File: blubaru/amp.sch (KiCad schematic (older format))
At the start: 20 parts, among them J1 TPA6112

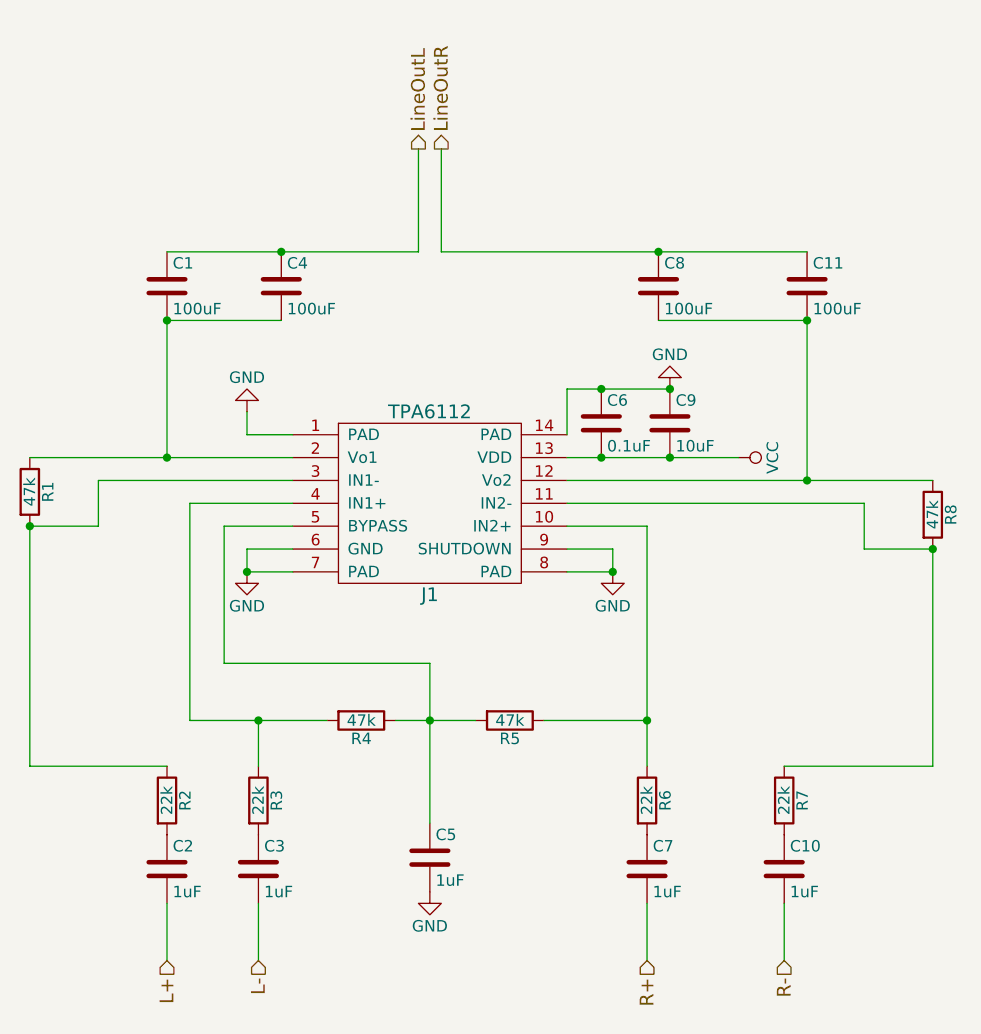
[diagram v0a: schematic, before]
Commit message: Put parts in the audio switch page.
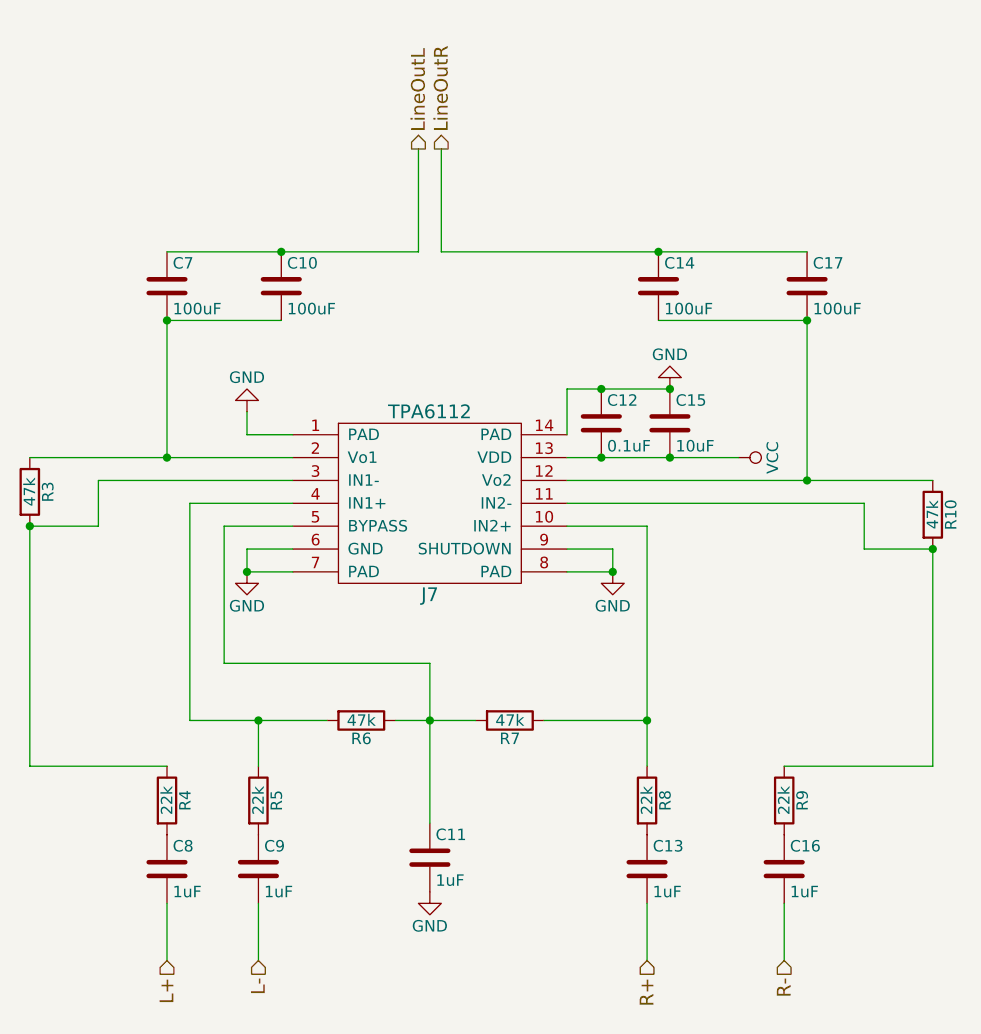
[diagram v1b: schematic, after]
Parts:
- renumbered C4 to C10, C5 to C11, C6 to C12, C7 to C13, C8 to C14, C9 to C15, C10 to C16, C11 to C17, C1 to C7, C2 to C8, C3 to C9, J1 to J7, R8 to R10, R1 to R3, R2 to R4, R3 to R5, R4 to R6, R5 to R7, R6 to R8, R7 to R9

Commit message: Create footprints for breakout boards
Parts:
- C10, C11, C12, C13, C14, C15, C16, C17, C7, C8, C9: footprint (none) -> Capacitors_THT:C_Disc_D5.0mm_W2.5mm_P2.50mm
- R10, R3, R4, R5, R6, R7, R8, R9: footprint (none) -> Resistors_THT:R_Axial_DIN0207_L6.3mm_D2.5mm_P7.62mm_Horizontal
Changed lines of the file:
@@
 encoding utf-8
 Sheet 8 8
-Title ""
-Date ""
+Title "Blubaru"
+Date "2017-02-28"
 Rev ""
 Comp ""
@@
 F 0 "C8" H 4175 5300 50  0000 L CNN
 F 1 "1uF" H 4175 5100 50  0000 L CNN
-F 2 "" H 4188 5050 50  0000 C CNN
+F 2 "Capacitors_THT:C_Disc_D5.0mm_W2.5mm_P2.50mm" H 4188 5050 50  0001 C CNN
 F 3 "" H 4150 5200 50  0000 C CNN
 	1    4150 5200
@@
 F 0 "C9" H 4575 5300 50  0000 L CNN
 F 1 "1uF" H 4575 5100 50  0000 L CNN
-F 2 "" H 4588 5050 50  0000 C CNN
+F 2 "Capacitors_THT:C_Disc_D5.0mm_W2.5mm_P2.50mm" H 4588 5050 50  0001 C CNN
 F 3 "" H 4550 5200 50  0000 C CNN
 	1    4550 5200
@@
 F 0 "C11" H 5325 5250 50  0000 L CNN
 F 1 "1uF" H 5325 5050 50  0000 L CNN
-F 2 "" H 5338 5000 50  0000 C CNN
+F 2 "Capacitors_THT:C_Disc_D5.0mm_W2.5mm_P2.50mm" H 5338 5000 50  0001 C CNN
 F 3 "" H 5300 5150 50  0000 C CNN
 	1    5300 5150
@@
 F 0 "C13" H 6275 5300 50  0000 L CNN
 F 1 "1uF" H 6275 5100 50  0000 L CNN
-F 2 "" H 6288 5050 50  0000 C CNN
+F 2 "Capacitors_THT:C_Disc_D5.0mm_W2.5mm_P2.50mm" H 6288 5050 50  0001 C CNN
 F 3 "" H 6250 5200 50  0000 C CNN
 	1    6250 5200
@@
 F 0 "C16" H 6875 5300 50  0000 L CNN
 F 1 "1uF" H 6875 5100 50  0000 L CNN
-F 2 "" H 6888 5050 50  0000 C CNN
+F 2 "Capacitors_THT:C_Disc_D5.0mm_W2.5mm_P2.50mm" H 6888 5050 50  0001 C CNN
 F 3 "" H 6850 5200 50  0000 C CNN
 	1    6850 5200
@@
 F 0 "C7" H 4175 2750 50  0000 L CNN
 F 1 "100uF" H 4175 2550 50  0000 L CNN
-F 2 "" H 4188 2500 50  0000 C CNN
+F 2 "Capacitors_THT:C_Disc_D5.0mm_W2.5mm_P2.50mm" H 4188 2500 50  0001 C CNN
 F 3 "" H 4150 2650 50  0000 C CNN
 	1    4150 2650
@@
 F 0 "C10" H 4675 2750 50  0000 L CNN
 F 1 "100uF" H 4675 2550 50  0000 L CNN
-F 2 "" H 4688 2500 50  0000 C CNN
+F 2 "Capacitors_THT:C_Disc_D5.0mm_W2.5mm_P2.50mm" H 4688 2500 50  0001 C CNN
 F 3 "" H 4650 2650 50  0000 C CNN
 	1    4650 2650
@@
 F 0 "C14" H 6325 2750 50  0000 L CNN
 F 1 "100uF" H 6325 2550 50  0000 L CNN
-F 2 "" H 6338 2500 50  0000 C CNN
+F 2 "Capacitors_THT:C_Disc_D5.0mm_W2.5mm_P2.50mm" H 6338 2500 50  0001 C CNN
 F 3 "" H 6300 2650 50  0000 C CNN
 	1    6300 2650
@@
 F 0 "C17" H 6975 2750 50  0000 L CNN
 F 1 "100uF" H 6975 2550 50  0000 L CNN
-F 2 "" H 6988 2500 50  0000 C CNN
+F 2 "Capacitors_THT:C_Disc_D5.0mm_W2.5mm_P2.50mm" H 6988 2500 50  0001 C CNN
 F 3 "" H 6950 2650 50  0000 C CNN
 	1    6950 2650
@@
 F 0 "C15" H 6375 3350 50  0000 L CNN
 F 1 "10uF" H 6375 3150 50  0000 L CNN
-F 2 "" H 6388 3100 50  0000 C CNN
+F 2 "Capacitors_THT:C_Disc_D5.0mm_W2.5mm_P2.50mm" H 6388 3100 50  0001 C CNN
 F 3 "" H 6350 3250 50  0000 C CNN
 	1    6350 3250
@@
 F 0 "C12" H 6075 3350 50  0000 L CNN
 F 1 "0.1uF" H 6075 3150 50  0000 L CNN
-F 2 "" H 6088 3100 50  0000 C CNN
+F 2 "Capacitors_THT:C_Disc_D5.0mm_W2.5mm_P2.50mm" H 6088 3100 50  0001 C CNN
 F 3 "" H 6050 3250 50  0000 C CNN
 	1    6050 3250
@@
 F 0 "R4" V 4230 4900 50  0000 C CNN
 F 1 "22k" V 4150 4900 50  0000 C CNN
-F 2 "" V 4080 4900 50  0000 C CNN
+F 2 "Resistors_THT:R_Axial_DIN0207_L6.3mm_D2.5mm_P7.62mm_Horizontal" V 4080 4900 50  0001 C CNN
 F 3 "" H 4150 4900 50  0000 C CNN
 	1    4150 4900
@@
 F 0 "R5" V 4630 4900 50  0000 C CNN
 F 1 "22k" V 4550 4900 50  0000 C CNN
-F 2 "" V 4480 4900 50  0000 C CNN
+F 2 "Resistors_THT:R_Axial_DIN0207_L6.3mm_D2.5mm_P7.62mm_Horizontal" V 4480 4900 50  0001 C CNN
 F 3 "" H 4550 4900 50  0000 C CNN
 	1    4550 4900
@@
 F 0 "R6" V 5080 4550 50  0000 C CNN
 F 1 "47k" V 5000 4550 50  0000 C CNN
-F 2 "" V 4930 4550 50  0000 C CNN
+F 2 "Resistors_THT:R_Axial_DIN0207_L6.3mm_D2.5mm_P7.62mm_Horizontal" V 4930 4550 50  0001 C CNN
 F 3 "" H 5000 4550 50  0000 C CNN
 	1    5000 4550
@@
 F 0 "R7" V 5730 4550 50  0000 C CNN
 F 1 "47k" V 5650 4550 50  0000 C CNN
-F 2 "" V 5580 4550 50  0000 C CNN
+F 2 "Resistors_THT:R_Axial_DIN0207_L6.3mm_D2.5mm_P7.62mm_Horizontal" V 5580 4550 50  0001 C CNN
 F 3 "" H 5650 4550 50  0000 C CNN
 	1    5650 4550
@@
 F 0 "R8" V 6330 4900 50  0000 C CNN
 F 1 "22k" V 6250 4900 50  0000 C CNN
-F 2 "" V 6180 4900 50  0000 C CNN
+F 2 "Resistors_THT:R_Axial_DIN0207_L6.3mm_D2.5mm_P7.62mm_Horizontal" V 6180 4900 50  0001 C CNN
 F 3 "" H 6250 4900 50  0000 C CNN
 	1    6250 4900
@@
 F 0 "R9" V 6930 4900 50  0000 C CNN
 F 1 "22k" V 6850 4900 50  0000 C CNN
-F 2 "" V 6780 4900 50  0000 C CNN
+F 2 "Resistors_THT:R_Axial_DIN0207_L6.3mm_D2.5mm_P7.62mm_Horizontal" V 6780 4900 50  0001 C CNN
 F 3 "" H 6850 4900 50  0000 C CNN
 	1    6850 4900
@@
 F 0 "R10" V 7580 3650 50  0000 C CNN
 F 1 "47k" V 7500 3650 50  0000 C CNN
-F 2 "" V 7430 3650 50  0000 C CNN
+F 2 "Resistors_THT:R_Axial_DIN0207_L6.3mm_D2.5mm_P7.62mm_Horizontal" V 7430 3650 50  0001 C CNN
 F 3 "" H 7500 3650 50  0000 C CNN
 	1    7500 3650
@@
 F 0 "R3" V 3630 3550 50  0000 C CNN
 F 1 "47k" V 3550 3550 50  0000 C CNN
-F 2 "" V 3480 3550 50  0000 C CNN
+F 2 "Resistors_THT:R_Axial_DIN0207_L6.3mm_D2.5mm_P7.62mm_Horizontal" V 3480 3550 50  0001 C CNN
 F 3 "" H 3550 3550 50  0000 C CNN
 	1    3550 3550
@@
 $EndComp
 $Comp
-L GND #PWR019
+L GND #PWR022
 U 1 1 5899599A
 P 6350 3100
-F 0 "#PWR019" H 6350 2850 50  0001 C CNN
+F 0 "#PWR022" H 6350 2850 50  0001 C CNN
 F 1 "GND" H 6350 2950 50  0000 C CNN
 F 2 "" H 6350 3100 50  0000 C CNN
@@
 $EndComp
 $Comp
-L GND #PWR020
+L GND #PWR023
 U 1 1 589959D6
 P 6100 3900
-F 0 "#PWR020" H 6100 3650 50  0001 C CNN
+F 0 "#PWR023" H 6100 3650 50  0001 C CNN
 F 1 "GND" H 6100 3750 50  0000 C CNN
 F 2 "" H 6100 3900 50  0000 C CNN
@@
 $EndComp
 $Comp
-L GND #PWR021
+L GND #PWR024
 U 1 1 58995A12
 P 4500 3200
-F 0 "#PWR021" H 4500 2950 50  0001 C CNN
+F 0 "#PWR024" H 4500 2950 50  0001 C CNN
 F 1 "GND" H 4500 3050 50  0000 C CNN
 F 2 "" H 4500 3200 50  0000 C CNN
@@
 $EndComp
 $Comp
-L GND #PWR022
+L GND #PWR025
 U 1 1 58995A8A
 P 4500 3900
-F 0 "#PWR022" H 4500 3650 50  0001 C CNN
+F 0 "#PWR025" H 4500 3650 50  0001 C CNN
 F 1 "GND" H 4500 3750 50  0000 C CNN
 F 2 "" H 4500 3900 50  0000 C CNN
@@
 $EndComp
 $Comp
-L VCC #PWR023
+L VCC #PWR026
 U 1 1 589A8C5A
 P 6650 3400
-F 0 "#PWR023" H 6650 3250 50  0001 C CNN
+F 0 "#PWR026" H 6650 3250 50  0001 C CNN
 F 1 "VCC" H 6650 3550 50  0000 C CNN
 F 2 "" H 6650 3400 50  0000 C CNN
@@
 $EndComp
 $Comp
-L GND #PWR024
+L GND #PWR027
 U 1 1 589AA8CC
 P 5300 5300
-F 0 "#PWR024" H 5300 5050 50  0001 C CNN
+F 0 "#PWR027" H 5300 5050 50  0001 C CNN
 F 1 "GND" H 5300 5150 50  0000 C CNN
 F 2 "" H 5300 5300 50  0000 C CNN

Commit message: Actually save the schematics that I had open.
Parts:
- J7: footprint (none) -> blubaru:TPA6112
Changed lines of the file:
@@
 F 0 "J7" H 5300 2400 60  0000 C CNN
 F 1 "TPA6112" H 5300 3200 60  0000 C CNN
-F 2 "" H 5300 3200 60  0001 C CNN
+F 2 "blubaru:TPA6112" H 5300 3200 60  0001 C CNN
 F 3 "" H 5300 3200 60  0001 C CNN
 	1    5300 3200

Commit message: Update footprints for passives.
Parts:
- C10, C14, C17, C7: footprint Capacitors_THT:C_Disc_D5.0mm_W2.5mm_P2.50mm -> Capacitors_THT:C_Rect_L4.6mm_W3.8mm_P2.50mm_MKS02_FKP02
- C15: footprint Capacitors_THT:C_Disc_D5.0mm_W2.5mm_P2.50mm -> Capacitors_THT:CP_Radial_D4.0mm_P1.50mm
- R10, R3, R4, R5, R6, R7, R8, R9: footprint Resistors_THT:R_Axial_DIN0207_L6.3mm_D2.5mm_P7.62mm_Horizontal -> Resistors_THT:R_Axial_DIN0204_L3.6mm_D1.6mm_P5.08mm_Horizontal
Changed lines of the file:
@@
 F 0 "C7" H 4175 2750 50  0000 L CNN
 F 1 "100uF" H 4175 2550 50  0000 L CNN
-F 2 "Capacitors_THT:C_Disc_D5.0mm_W2.5mm_P2.50mm" H 4188 2500 50  0001 C CNN
+F 2 "Capacitors_THT:C_Rect_L4.6mm_W3.8mm_P2.50mm_MKS02_FKP02" H 4188 2500 50  0001 C CNN
 F 3 "" H 4150 2650 50  0000 C CNN
 	1    4150 2650
@@
 F 0 "C10" H 4675 2750 50  0000 L CNN
 F 1 "100uF" H 4675 2550 50  0000 L CNN
-F 2 "Capacitors_THT:C_Disc_D5.0mm_W2.5mm_P2.50mm" H 4688 2500 50  0001 C CNN
+F 2 "Capacitors_THT:C_Rect_L4.6mm_W3.8mm_P2.50mm_MKS02_FKP02" H 4688 2500 50  0001 C CNN
 F 3 "" H 4650 2650 50  0000 C CNN
 	1    4650 2650
@@
 F 0 "C14" H 6325 2750 50  0000 L CNN
 F 1 "100uF" H 6325 2550 50  0000 L CNN
-F 2 "Capacitors_THT:C_Disc_D5.0mm_W2.5mm_P2.50mm" H 6338 2500 50  0001 C CNN
+F 2 "Capacitors_THT:C_Rect_L4.6mm_W3.8mm_P2.50mm_MKS02_FKP02" H 6338 2500 50  0001 C CNN
 F 3 "" H 6300 2650 50  0000 C CNN
 	1    6300 2650
@@
 F 0 "C17" H 6975 2750 50  0000 L CNN
 F 1 "100uF" H 6975 2550 50  0000 L CNN
-F 2 "Capacitors_THT:C_Disc_D5.0mm_W2.5mm_P2.50mm" H 6988 2500 50  0001 C CNN
+F 2 "Capacitors_THT:C_Rect_L4.6mm_W3.8mm_P2.50mm_MKS02_FKP02" H 6988 2500 50  0001 C CNN
 F 3 "" H 6950 2650 50  0000 C CNN
 	1    6950 2650
@@
 F 0 "C15" H 6375 3350 50  0000 L CNN
 F 1 "10uF" H 6375 3150 50  0000 L CNN
-F 2 "Capacitors_THT:C_Disc_D5.0mm_W2.5mm_P2.50mm" H 6388 3100 50  0001 C CNN
+F 2 "Capacitors_THT:CP_Radial_D4.0mm_P1.50mm" H 6388 3100 50  0001 C CNN
 F 3 "" H 6350 3250 50  0000 C CNN
 	1    6350 3250
@@
 F 0 "R4" V 4230 4900 50  0000 C CNN
 F 1 "22k" V 4150 4900 50  0000 C CNN
-F 2 "Resistors_THT:R_Axial_DIN0207_L6.3mm_D2.5mm_P7.62mm_Horizontal" V 4080 4900 50  0001 C CNN
+F 2 "Resistors_THT:R_Axial_DIN0204_L3.6mm_D1.6mm_P5.08mm_Horizontal" V 4080 4900 50  0001 C CNN
 F 3 "" H 4150 4900 50  0000 C CNN
 	1    4150 4900
@@
 F 0 "R5" V 4630 4900 50  0000 C CNN
 F 1 "22k" V 4550 4900 50  0000 C CNN
-F 2 "Resistors_THT:R_Axial_DIN0207_L6.3mm_D2.5mm_P7.62mm_Horizontal" V 4480 4900 50  0001 C CNN
+F 2 "Resistors_THT:R_Axial_DIN0204_L3.6mm_D1.6mm_P5.08mm_Horizontal" V 4480 4900 50  0001 C CNN
 F 3 "" H 4550 4900 50  0000 C CNN
 	1    4550 4900
@@
 F 0 "R6" V 5080 4550 50  0000 C CNN
 F 1 "47k" V 5000 4550 50  0000 C CNN
-F 2 "Resistors_THT:R_Axial_DIN0207_L6.3mm_D2.5mm_P7.62mm_Horizontal" V 4930 4550 50  0001 C CNN
+F 2 "Resistors_THT:R_Axial_DIN0204_L3.6mm_D1.6mm_P5.08mm_Horizontal" V 4930 4550 50  0001 C CNN
 F 3 "" H 5000 4550 50  0000 C CNN
 	1    5000 4550
@@
 F 0 "R7" V 5730 4550 50  0000 C CNN
 F 1 "47k" V 5650 4550 50  0000 C CNN
-F 2 "Resistors_THT:R_Axial_DIN0207_L6.3mm_D2.5mm_P7.62mm_Horizontal" V 5580 4550 50  0001 C CNN
+F 2 "Resistors_THT:R_Axial_DIN0204_L3.6mm_D1.6mm_P5.08mm_Horizontal" V 5580 4550 50  0001 C CNN
 F 3 "" H 5650 4550 50  0000 C CNN
 	1    5650 4550
@@
 F 0 "R8" V 6330 4900 50  0000 C CNN
 F 1 "22k" V 6250 4900 50  0000 C CNN
-F 2 "Resistors_THT:R_Axial_DIN0207_L6.3mm_D2.5mm_P7.62mm_Horizontal" V 6180 4900 50  0001 C CNN
+F 2 "Resistors_THT:R_Axial_DIN0204_L3.6mm_D1.6mm_P5.08mm_Horizontal" V 6180 4900 50  0001 C CNN
 F 3 "" H 6250 4900 50  0000 C CNN
 	1    6250 4900
@@
 F 0 "R9" V 6930 4900 50  0000 C CNN
 F 1 "22k" V 6850 4900 50  0000 C CNN
-F 2 "Resistors_THT:R_Axial_DIN0207_L6.3mm_D2.5mm_P7.62mm_Horizontal" V 6780 4900 50  0001 C CNN
+F 2 "Resistors_THT:R_Axial_DIN0204_L3.6mm_D1.6mm_P5.08mm_Horizontal" V 6780 4900 50  0001 C CNN
 F 3 "" H 6850 4900 50  0000 C CNN
 	1    6850 4900
@@
 F 0 "R10" V 7580 3650 50  0000 C CNN
 F 1 "47k" V 7500 3650 50  0000 C CNN
-F 2 "Resistors_THT:R_Axial_DIN0207_L6.3mm_D2.5mm_P7.62mm_Horizontal" V 7430 3650 50  0001 C CNN
+F 2 "Resistors_THT:R_Axial_DIN0204_L3.6mm_D1.6mm_P5.08mm_Horizontal" V 7430 3650 50  0001 C CNN
 F 3 "" H 7500 3650 50  0000 C CNN
 	1    7500 3650
@@
 F 0 "R3" V 3630 3550 50  0000 C CNN
 F 1 "47k" V 3550 3550 50  0000 C CNN
-F 2 "Resistors_THT:R_Axial_DIN0207_L6.3mm_D2.5mm_P7.62mm_Horizontal" V 3480 3550 50  0001 C CNN
+F 2 "Resistors_THT:R_Axial_DIN0204_L3.6mm_D1.6mm_P5.08mm_Horizontal" V 3480 3550 50  0001 C CNN
 F 3 "" H 3550 3550 50  0000 C CNN
 	1    3550 3550
